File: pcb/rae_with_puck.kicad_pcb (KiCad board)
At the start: 2 copper layers, 126.9 x 99.3 mm, 40 parts

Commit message: add gerber files
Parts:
- moved S25 2.07 mm to (134.4, -71.2)
- moved S26 2.07 mm to (134.4, -71.2)
- moved S27 2.07 mm to (134.4, -88.2)
- moved S28 2.07 mm to (134.4, -88.2)
- moved S29 2.07 mm to (134.4, -105.2)
- moved S30 2.07 mm to (134.4, -105.2)
- moved REF** 0.60 mm to (103.8, -88.1)
- moved S19 0.60 mm to (115.4, -72.7)
- moved S20 0.60 mm to (115.4, -72.7)
- moved S21 0.60 mm to (115.4, -89.7)
- moved S22 0.60 mm to (115.4, -89.7)
- moved S23 0.60 mm to (115.4, -106.7)
- moved S24 0.60 mm to (115.4, -106.7)
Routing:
- net P1: track 135.9 -> 141.9 mm
- net P18: track 132.8 -> 138.9 mm
- net P15: track 146.3 -> 152.4 mm
- net P14: track 84.3 -> 89.4 mm
- net P10: track 108.9 -> 112.6 mm
- net P16: track 96.0 -> 99.8 mm
- net P8: track 90.5 -> 86.8 mm
- net P4: track 169.1 -> 172.2 mm
- net P6: track 154.1 -> 157.1 mm
- net P3: track 136.5 -> 139.5 mm
- net P2: track 154.0 -> 157.0 mm
- net P19: track 61.0 -> 63.0 mm
- net P5: track 150.9 -> 152.9 mm
- net P20: track 47.0 -> 47.9 mm
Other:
- outline, holes or cut-outs redrawn

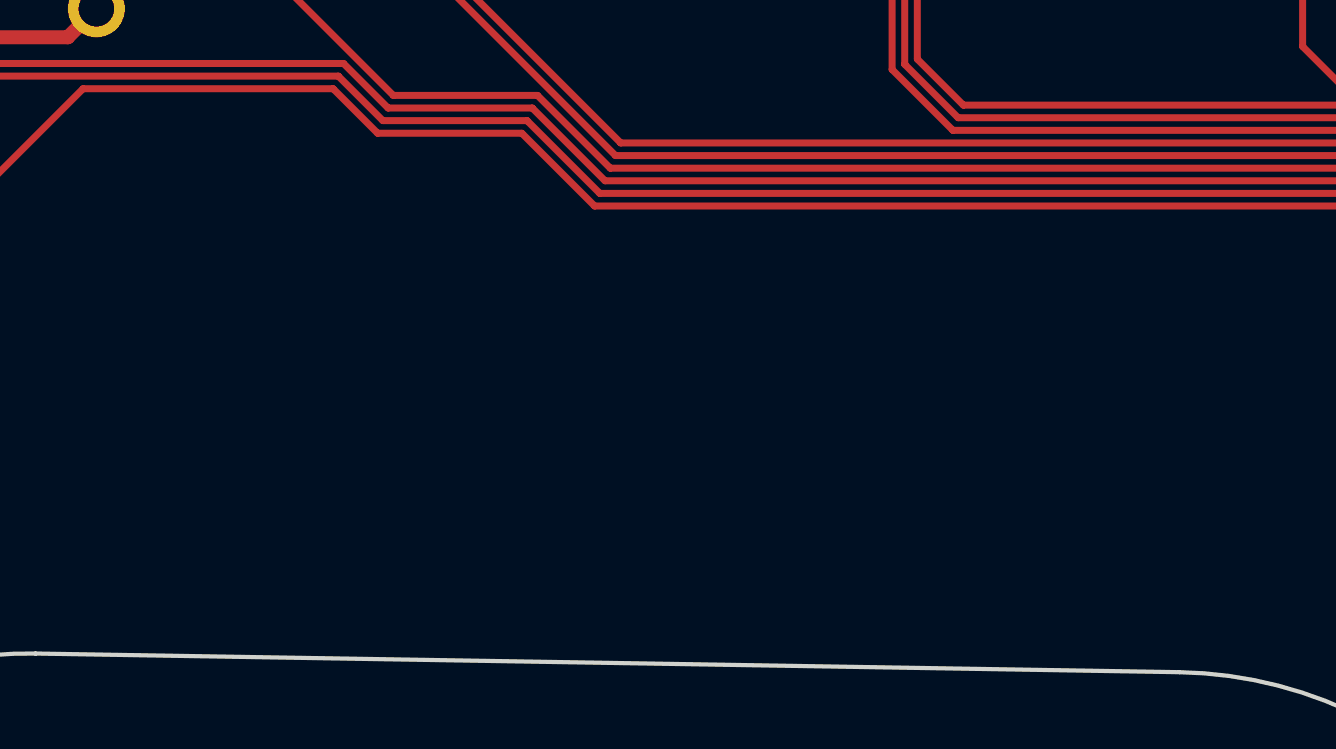
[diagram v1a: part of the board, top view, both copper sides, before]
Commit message: add logo
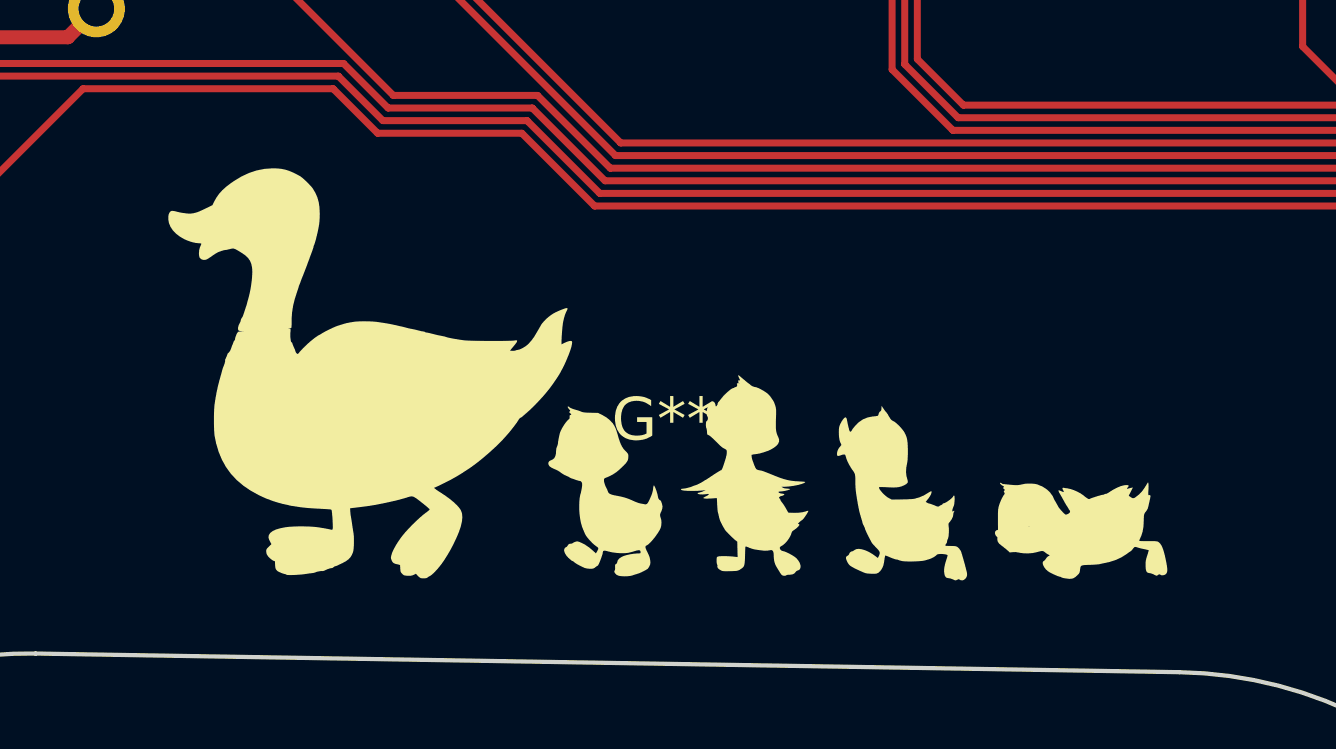
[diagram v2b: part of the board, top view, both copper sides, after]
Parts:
- added G***: LOGO, LOGO, F.Cu at (99.1, -50.8)
- added G***: LOGO, LOGO, B.Cu at (99.1, -50.8)
